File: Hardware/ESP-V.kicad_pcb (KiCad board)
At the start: 2 copper layers, 29.1 x 48.2 mm, 54 parts, among them J1 USB_C_Receptacle_USB2.0, J2 Conn_01x16_Male, J3 Conn_01x14_Female, J4 Conn_Coaxial, U1 AT25xxx-MA, U2 AP7333-33SRG-7, U3 AP7333-33SRG-7, U4 ESP32-C3, U5 CH552G, Y1 40MHz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

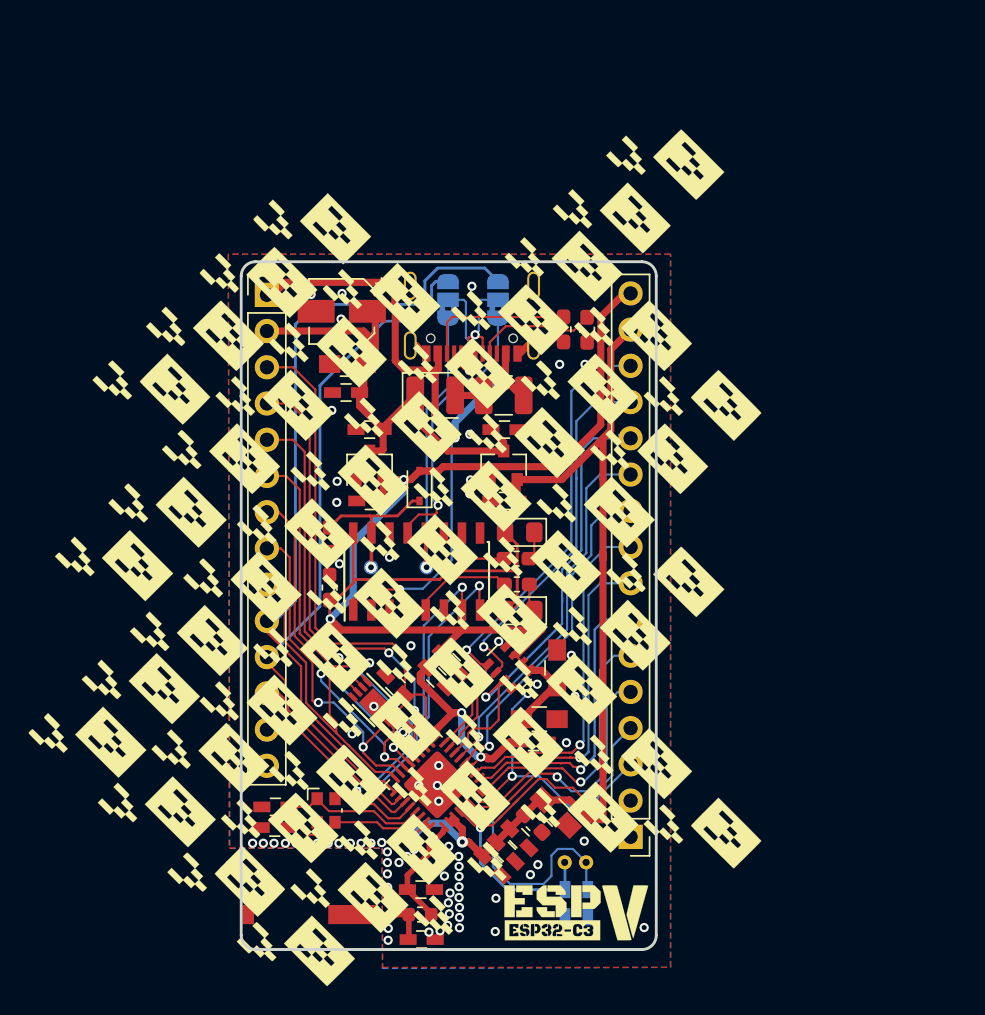
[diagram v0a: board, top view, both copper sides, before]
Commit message: redesigning to take module
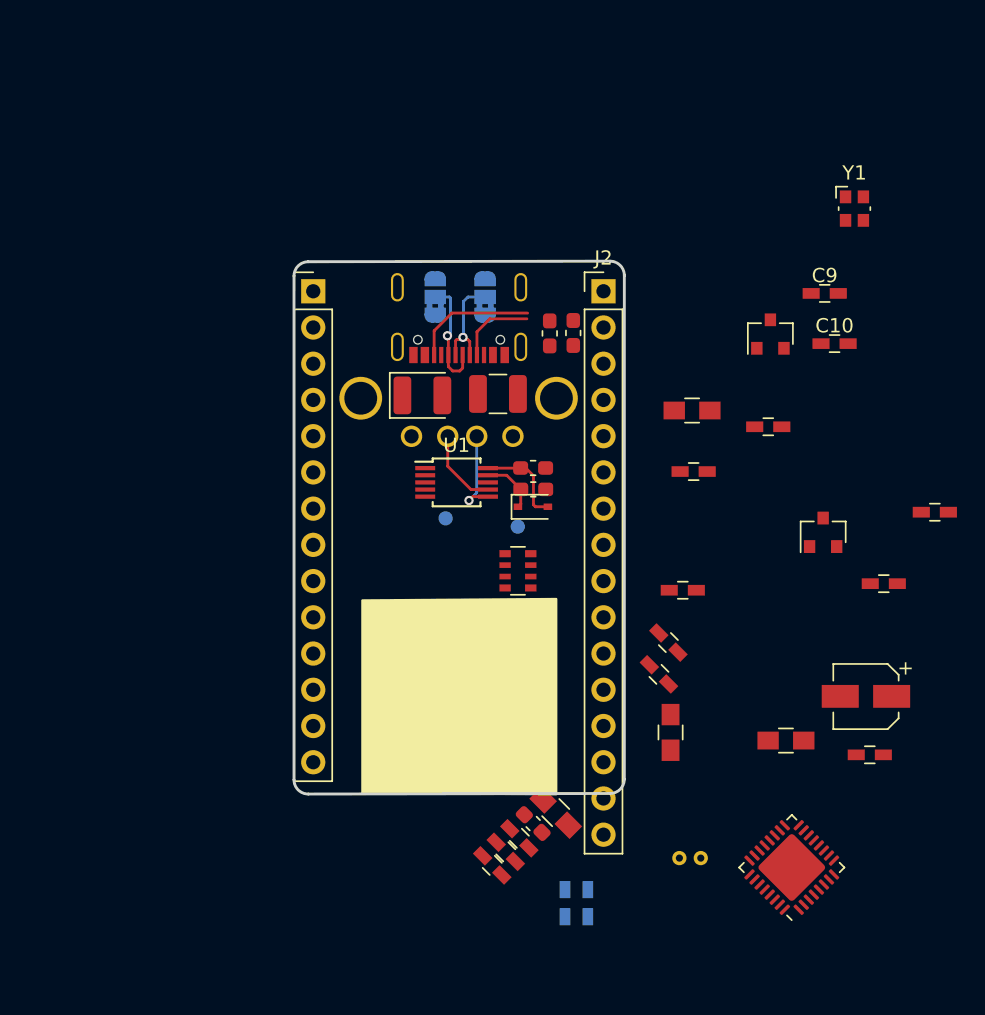
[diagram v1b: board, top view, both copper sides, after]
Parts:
- removed C21, C22: C_Small, Capacitors_SMD:C_0603_HandSoldering
- removed C6: 100nF, Capacitors_SMD:C_0603_HandSoldering
- removed D2, D3: LED_ALT, LED_SMD:LED_0805_2012Metric_Pad1.15x1.40mm_HandSolder
- removed G***: LOGO, art and silk:frontsilk
- removed G***: LOGO, art and silk:backsilk
- removed L2: L_Small, Inductor_SMD:L_0603_1608Metric
- removed R3, R4: 1k, Resistor_SMD:R_0603_1608Metric_Pad1.05x0.95mm_HandSolder
- removed U5: CH552G, Housings_SOIC:SOIC-16_3.9x9.9mm_Pitch1.27mm
- J4: value Conn_Coaxial -> USB_A; footprint footprint:ACAG0801-2450-T -> Connectors:USB_A; moved to B.Cu
- U1: value AT25xxx-MA -> CH552E; footprint Package_DFN_QFN:DFN-8-1EP_3x2mm_P0.5mm_EP1.75x1.45mm -> Package_SO:MSOP-10_3x3mm_P0.5mm
- Y2: footprint footprint:Crystal_DS10_D1.0mm_L4.3mm_Horizontalnosilk -> Crystal:Crystal_DS10_D1.0mm_L4.3mm_Horizontal
- moved Y1 56.1 mm to (131.9, 72.8)
- moved C9 52.7 mm to (129.8, 78.8), turned to 0 degrees
- moved C10 51.9 mm to (130.5, 82.3), turned to 0 degrees
- moved C1 45.6 mm to (132.7, 107.0)
- moved C7 39.6 mm to (137.5, 94.1)
- moved J2 38.3 mm to (114.3, 78.6), turned to 0 degrees
- moved J4 36.0 mm to (100.8, 88.8)
- moved U2 29.6 mm to (126.0, 81.6)
- moved C5 28.7 mm to (133.9, 99.1)
- moved U4 25.5 mm to (127.5, 119.0)
- moved C3 25.0 mm to (120.6, 91.2)
- moved C4 24.7 mm to (119.9, 99.6)
- moved C2 24.4 mm to (120.5, 87.0)
- moved C23 23.6 mm to (133.0, 111.1)
- moved U3 22.9 mm to (129.7, 95.5)
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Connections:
- J1 pad 1: GND -> (no net)
- J1 pad A8: Net-(J1-PadA8) -> (no net)
- J1 pad B8: Net-(J1-PadB8) -> (no net)
- J2 pad 1: GND -> +3V3
- J2 pad 15: +3.3VA -> GND
- J2 pad 16: +3V3 -> GND
- J2 pad 2: GND -> +3.3VA
- J4 pad 1: Net-(C22-Pad1) -> VBUS
- J4 pad 2: (no net) -> /CHUSB-
- JP1 pad 1: /CHUSB- -> /ESPUSB-
- JP1 pad 3: /ESPUSB- -> /CHUSB-
- JP2 pad 1: /CHUSB+ -> /ESPUSB+
- JP2 pad 3: /ESPUSB+ -> /CHUSB+
- U1 pad 1: /GP14 -> (no net)
- U1 pad 2: /GP17 -> /BLSEL
- U1 pad 3: /GP13 -> /ESP_TX
- U1 pad 4: GND -> /ESP_RX
- U1 pad 5: /GP16 -> +3V3
- U1 pad 6: /GP15 -> /CHUSB+
- U1 pad 7: /GP12 -> /CHUSB-
- U1 pad 8: /GP11 -> GND
- U1 pad 9: GND -> Net-(C26-Pad1)
- U4 pad 1: /ANT -> (no net)
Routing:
- net +3V3: track 124.3 -> 6.53 mm, vias 4 -> 0
- net +3.3VA: track 66.0 -> 0.00 mm, vias 2 -> 0
- net /ESPUSB-: track 55.1 -> 0.00 mm
- net VBUS: track 51.7 -> 0.00 mm, vias 3 -> 0
- net /ESPUSB+: track 48.4 -> 0.00 mm
- net /GP11: track 37.3 -> 0.00 mm
- net VDD: track 35.2 -> 0.00 mm
- net /GP10: track 34.9 -> 0.00 mm, vias 1 -> 0
- net /GP01: track 34.7 -> 0.00 mm, vias 2 -> 0
- net /GP12: track 34.1 -> 0.00 mm, vias 2 -> 0
- net /ESP_RX: track 34.1 -> 0.00 mm, vias 2 -> 0
- net /GP08: track 33.8 -> 0.00 mm, vias 1 -> 0
- net /ESP_TX: track 32.6 -> 0.00 mm, vias 2 -> 0
- net /BLSEL: track 32.2 -> 0.00 mm, vias 1 -> 0
- net /GP13: track 30.3 -> 0.00 mm, vias 3 -> 0
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- removed copper zone on B.Cu, net GND
- removed copper zone on F.Cu, net GND
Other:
- board size 29.1 x 48.2 mm -> 23.2 x 37.4 mm

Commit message: v1.1 ready to order
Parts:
- removed C1: 100uF, Capacitors_SMD:CP_Elec_4x4.5
- removed C10, C15, C18, C9: 10nF, Capacitors_SMD:C_0603_HandSoldering
- removed C11, C12: 22uF 0805, Capacitors_SMD:C_0805_HandSoldering
- removed C13, C3, C5, C8: 1uF, Capacitors_SMD:C_0603_HandSoldering
- removed C14, C2: 10uF, Capacitors_SMD:C_0805_HandSoldering
- removed C16: 100nF, Capacitors_SMD:C_0603_HandSoldering
- removed C17: 10uF, Capacitors_SMD:C_0603_HandSoldering
- removed C19: 10pF, Capacitors_SMD:C_0603_HandSoldering
- removed C24: 100nF, Capacitor_SMD:C_0603_1608Metric_Pad1.05x0.95mm_HandSolder
- removed U4: ESP32-C3, Package_DFN_QFN:QFN-32-1EP_5x5mm_P0.5mm_EP3.45x3.45mm
- removed Y1: 40MHz, Crystal:Crystal_SMD_Abracon_ABM10-4Pin_2.5x2.0mm
- removed Y2: 32k, Crystal:Crystal_DS10_D1.0mm_L4.3mm_Horizontal
- added D2: LED, LED_SMD:LED_0603_1608Metric_Castellated, F.Cu at (113.3, 78.6)
- added G***: LOGO, art and silk:frontsilk, F.Cu at (110.4, 90.2)
- added G***: LOGO, art and silk:frontv11, B.Cu at (104.3, 94.5)
- added R3: R_Small, Resistor_SMD:R_0603_1608Metric_Pad1.05x0.95mm_HandSolder, F.Cu at (111.7, 78.6)
- C20: value 1uF -> 10uF; footprint Capacitors_SMD:C_0603_HandSoldering -> Capacitor_SMD:C_0805_2012Metric_Pad1.15x1.40mm_HandSolder
- D1: footprint Diode_SMD:D_1210_3225Metric -> Diode_SMD:D_SOD-323
- J2: value Conn_01x16_Male -> Conn_01x10_Female; footprint Connector_PinHeader_2.54mm:PinHeader_1x16_P2.54mm_Vertical -> Connector_PinSocket_2.54mm:PinSocket_1x10_P2.54mm_Vertical
- J3: value Conn_01x14_Female -> Conn_01x10_Female; footprint Connector_PinHeader_2.54mm:PinHeader_1x14_P2.54mm_Vertical -> Connector_PinSocket_2.54mm:PinSocket_1x10_P2.54mm_Vertical
- L1: footprint Inductor_SMD:L_1210_3225Metric -> Inductor_SMD:L_0805_2012Metric_Pad1.15x1.40mm_HandSolder
- U2: value AP7333-33SRG-7 -> NCP1117-3.3_SOT223; footprint TO_SOT_Packages_SMD:SOT-23 -> Package_TO_SOT_SMD:SOT-223-3_TabPin2
- U3: value AP7333-33SRG-7 -> ESP32-C3-MINI-1; footprint TO_SOT_Packages_SMD:SOT-23 -> footprint:ESP32-c3-mini1
- moved C7 29.7 mm to (108.1, 97.8), turned to 270 degrees
- moved C23 29.4 mm to (106.7, 97.8), turned to 270 degrees
- moved U2 28.4 mm to (101.5, 96.1), turned to 180 degrees
- moved U3 27.1 mm to (104.5, 105.4), turned to 180 degrees
- moved C4 21.3 mm to (100.2, 91.4)
- moved R1 15.1 mm to (97.4, 78.5), turned to 270 degrees
- moved TP1 11.4 mm to (109.6, 85.1), turned to 90 degrees
- moved C20 11.2 mm to (110.0, 97.8), turned to 270 degrees
- moved TP2 10.4 mm to (111.1, 85.1)
- moved L1 8.99 mm to (98.2, 88.1), turned to 90 degrees
- moved J3 7.16 mm to (95.3, 85.6)
- moved J2 7.12 mm to (113.1, 85.6)
- moved C26 4.78 mm to (110.8, 87.9), turned to 90 degrees
- moved RN1 4.62 mm to (109.7, 93.8)
- moved JP1 4.10 mm to (101.9, 79.0)
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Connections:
- J1 pad 1: (no net) -> GND
- J1 pad A8: (no net) -> Net-(J1-PadA8)
- J1 pad B8: (no net) -> Net-(J1-PadB8)
- J2 pad 10: /GP06 -> /GP07
- J2 pad 2: +3.3VA -> /ESP_ENABLE
- J2 pad 3: /ESP_ENABLE -> /GP00
- J2 pad 4: /GP00 -> /GP01
- J2 pad 5: /GP01 -> /GP02
- J2 pad 6: /GP02 -> /GP03
- J2 pad 7: /GP03 -> /GP04
- J2 pad 8: /GP04 -> /GP05
- J2 pad 9: /GP05 -> /GP06
- J3 pad 10: /ESPUSB- -> GND
- J3 pad 3: /GP11 -> /GP08
- J3 pad 4: /GP12 -> /BLSEL
- J3 pad 5: /GP13 -> /GP10
- J3 pad 6: /GP14 -> /ESPUSB-
- J3 pad 7: /GP15 -> /ESPUSB+
- J3 pad 8: /GP16 -> /ESP_RX
- J3 pad 9: /GP17 -> /ESP_TX
- RN1 pad 1: /GP10 -> Net-(RN1-Pad1)
- RN1 pad 8: GND -> Net-(RN1-Pad8)
- U1 pad 1: (no net) -> /ESP_ENABLE
- U3 pad 2: +3.3VA -> GND
- U3 pad 3: VDD -> +3V3
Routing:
- net +3V3: track 6.53 -> 57.5 mm, vias 0 -> 1
- net /ESPUSB+: track 0.00 -> 45.3 mm
- net /BLSEL: track 0.00 -> 32.8 mm, vias 0 -> 3
- net /ESP_ENABLE: track 0.00 -> 30.4 mm, vias 0 -> 4
- net /ESP_TX: track 0.00 -> 29.6 mm, vias 0 -> 1
- net /ESP_RX: track 0.00 -> 29.0 mm, vias 0 -> 1
- net /ESPUSB-: track 0.00 -> 28.3 mm
- net VBUS: track 0.00 -> 23.0 mm, vias 0 -> 1
- net /GP08: track 0.00 -> 22.3 mm, vias 0 -> 3
- net /GP04: track 0.00 -> 18.8 mm, vias 0 -> 1
- net /GP00: track 0.00 -> 18.0 mm, vias 0 -> 1
- net /GP05: track 0.00 -> 17.6 mm, vias 0 -> 1
- net /GP07: track 0.00 -> 16.6 mm, vias 0 -> 1
- net /GP06: track 0.00 -> 16.5 mm, vias 0 -> 1
- net /GP10: track 0.00 -> 15.6 mm, vias 0 -> 2
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- added copper zone on B.Cu, net GND
- added copper zone on F.Cu, net GND
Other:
- board size 23.2 x 37.4 mm -> 20.9 x 34.8 mm
- board text removed: "V1.0"
